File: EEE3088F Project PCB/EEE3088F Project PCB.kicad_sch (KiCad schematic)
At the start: 78 parts, among them IC1 74LVC1G04SE-7, J1 JST PH 2.00mm connector, J3 TYPE-C-31-M-12, SW1 SS12D07VG5 087, U1 DRV8833PWR, U10 LM7805L-TF3-T, U11 TC4056A., U2 DRV8833PWPR, U3 INA219AxD, U4 CH224K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

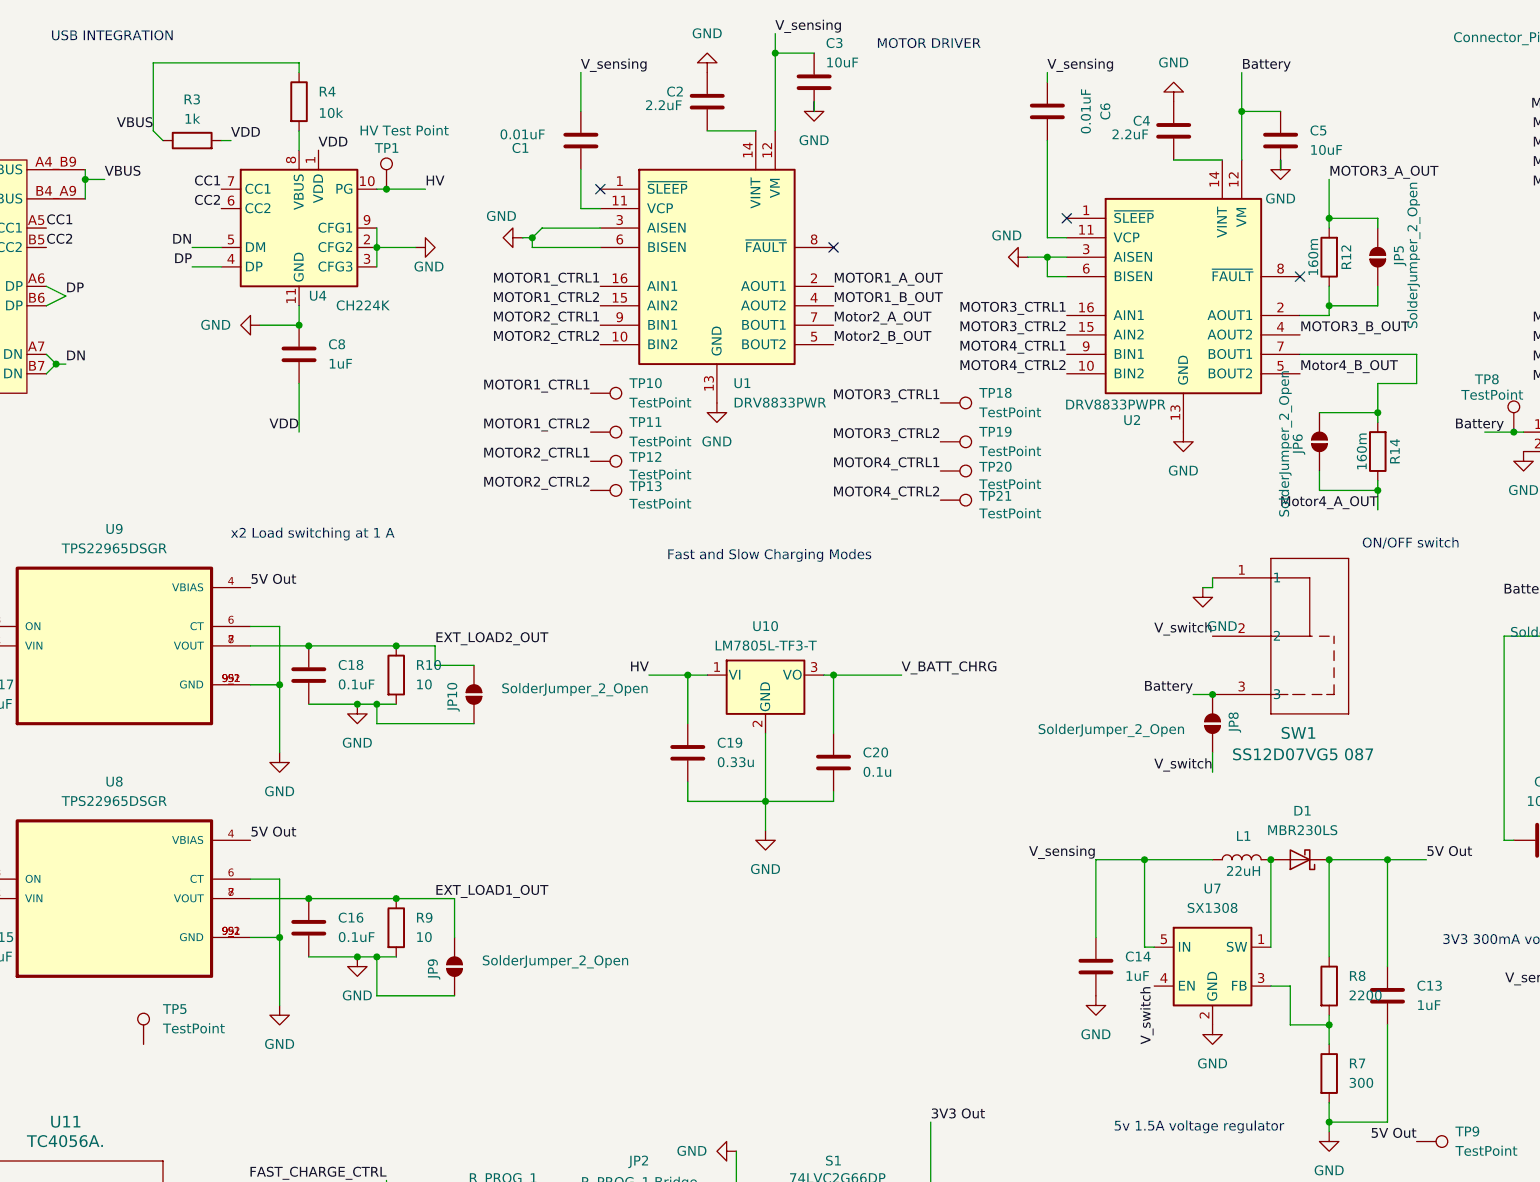
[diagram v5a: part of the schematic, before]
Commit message: Adjusted arrangments on board, and assigned all JLCP part numbers
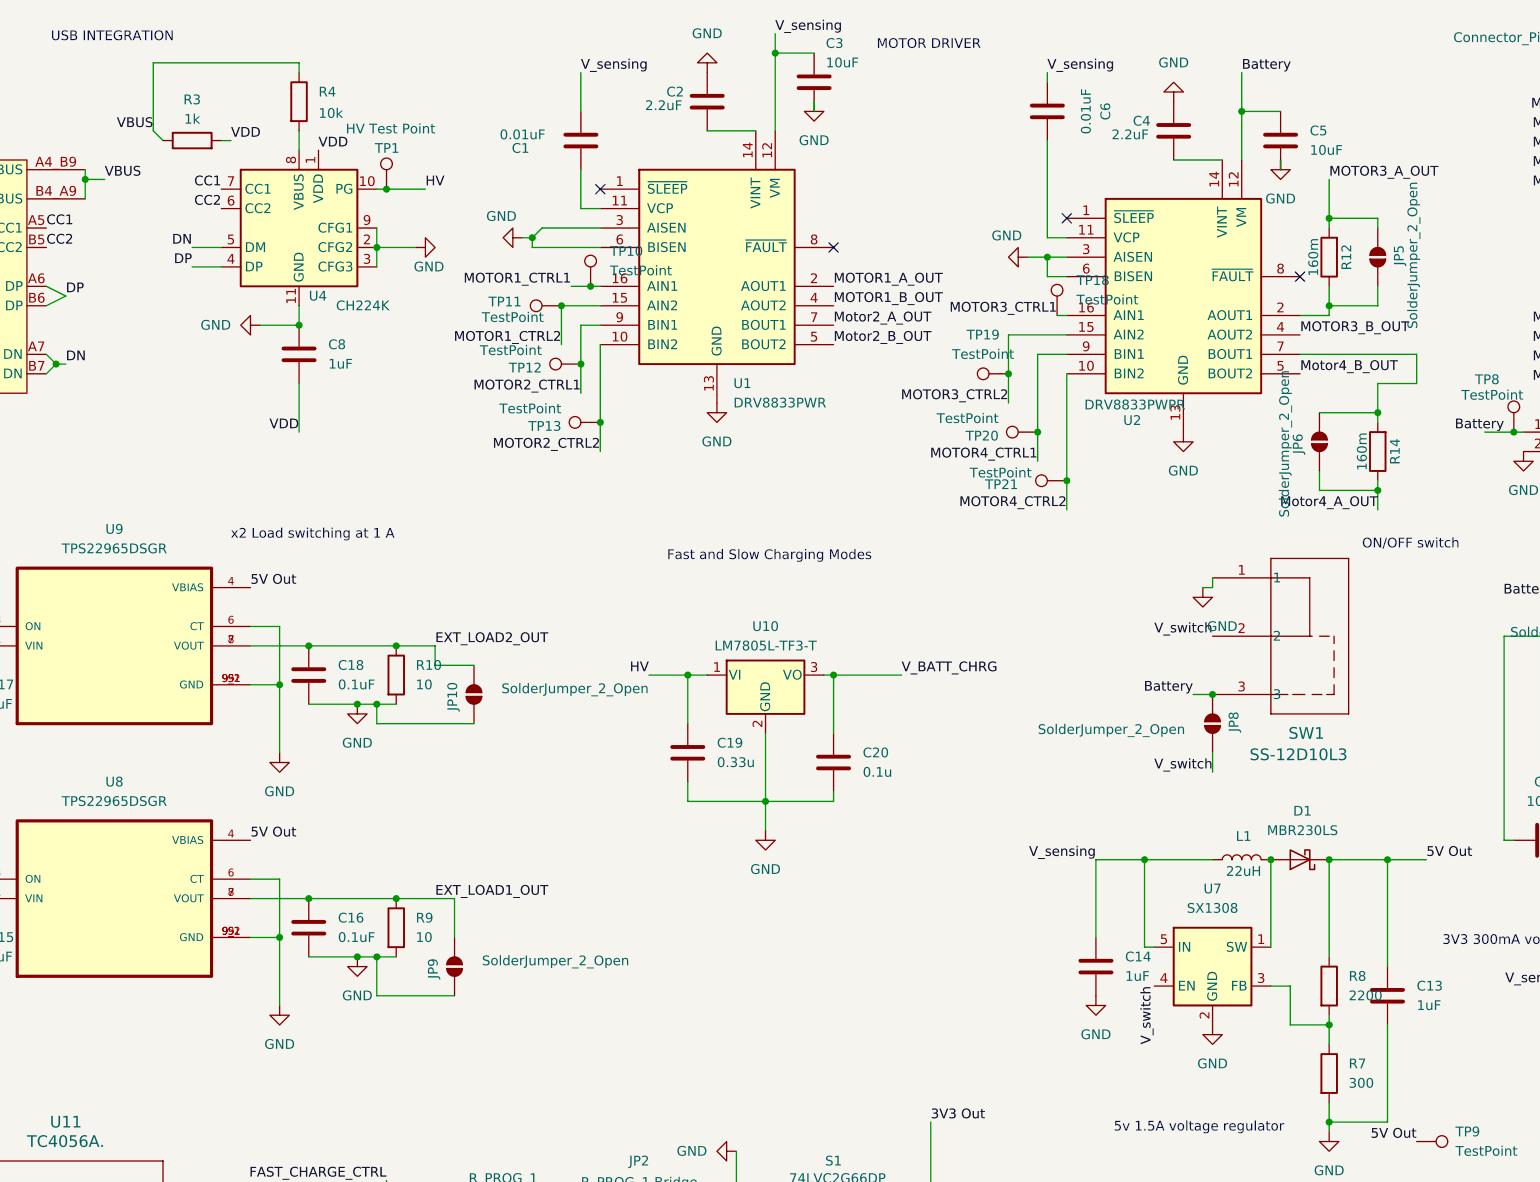
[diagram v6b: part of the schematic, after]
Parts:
- removed TP5: TestPoint, symbol Connector:TestPoint
- SW1: value SS12D07VG5 087 -> SS-12D10L3
- TP10, TP11, TP12, TP13, TP18, TP19, TP20, TP21, TP8: footprint (none) -> TestPoint:TestPoint_Pad_1.0x1.0mm
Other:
- moved on the sheet: TP10, TP11, TP12, TP13, TP18, TP19, TP20, TP21

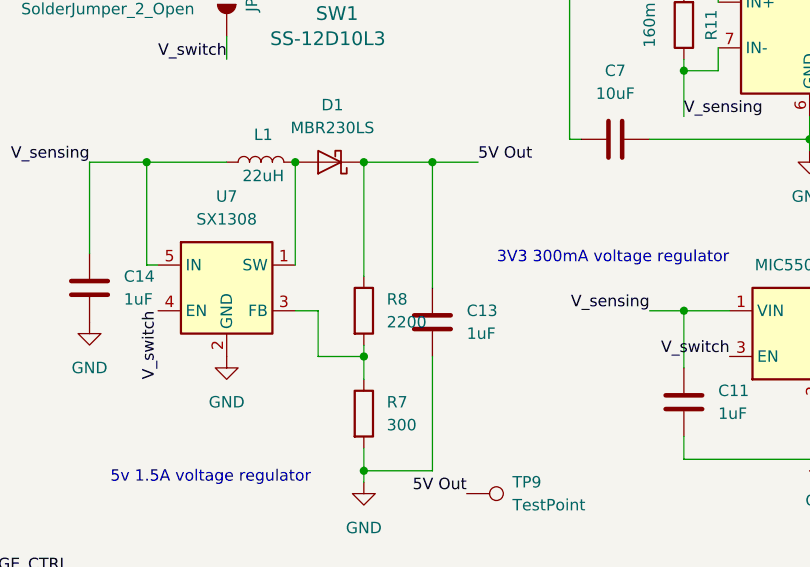
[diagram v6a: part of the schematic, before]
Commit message: adjusted position of 2*16 connector
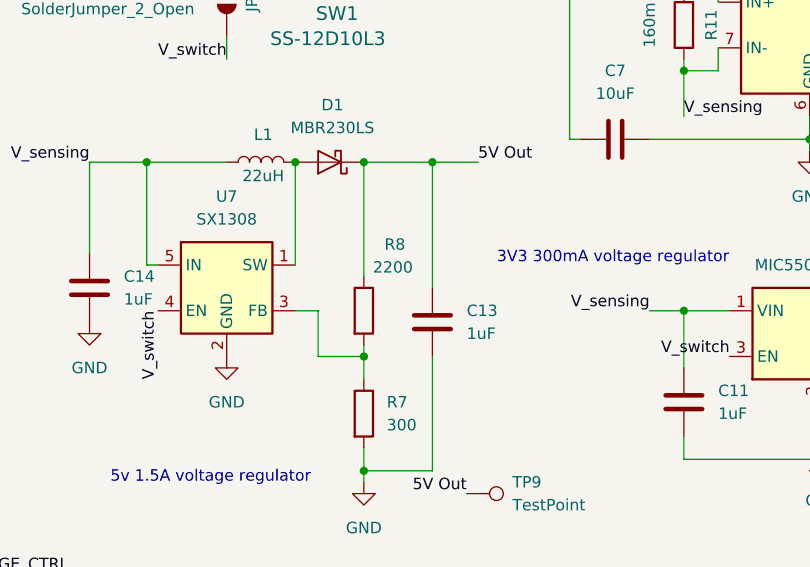
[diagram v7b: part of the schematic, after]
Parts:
- C11, C12, C13, C14, C15, C17: footprint Capacitor_SMD:C_0805_2012Metric_Pad1.18x1.45mm_HandSolder -> exported_footprints:CAPC3216X180N
- C7: footprint Capacitor_SMD:C_0805_2012Metric_Pad1.18x1.45mm_HandSolder -> Capacitor_SMD:C_0402_1005Metric_Pad0.74x0.62mm_HandSolder
- R7: footprint Resistor_SMD:R_0402_1005Metric_Pad0.72x0.64mm_HandSolder -> Resistor_SMD:R_0805_2012Metric_Pad1.20x1.40mm_HandSolder
- R8: footprint Resistor_SMD:R_0402_1005Metric_Pad0.72x0.64mm_HandSolder -> Resistor_SMD:R_0603_1608Metric_Pad0.98x0.95mm_HandSolder
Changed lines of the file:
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@@
 		(polyline
 			(pts
-				(xy 228.6 114.3) (xy 167.64 114.3) (xy 167.64 165.735) (xy 285.75 165.1) (xy 285.75 129.54) (xy 228.6 129.54)
+				(xy 222.25 12.7) (xy 222.25 78.74) (xy 284.48 78.74) (xy 284.48 12.7)
 			)
 			(stroke
@@
 		(polyline
 			(pts
-				(xy 222.25 12.7) (xy 222.25 78.74) (xy 284.48 78.74) (xy 284.48 12.7)
+				(xy 12.7 78.74) (xy 11.43 153.67) (xy 106.68 152.7175) (xy 106.68 78.4225)
 			)
 			(stroke
@@
 		(polyline
 			(pts
-				(xy 167.64 78.74) (xy 167.64 114.3) (xy 228.6 114.3) (xy 228.6 78.74)
+				(xy 93.98 12.7) (xy 93.98 78.74) (xy 222.25 78.74) (xy 222.25 12.7)
 			)
 			(stroke
@@
 		(polyline
 			(pts
-				(xy 93.98 12.7) (xy 93.98 78.74) (xy 222.25 78.74) (xy 222.25 12.7)
+				(xy 167.64 78.74) (xy 167.64 114.3) (xy 228.6 114.3) (xy 228.6 78.74)
 			)
 			(stroke
@@
 		(polyline
 			(pts
-				(xy 12.7 78.74) (xy 11.43 153.67) (xy 106.68 152.7175) (xy 106.68 78.4225)
+				(xy 228.6 114.3) (xy 167.64 114.3) (xy 167.64 165.735) (xy 285.75 165.1) (xy 285.75 129.54) (xy 228.6 129.54)
 			)
 			(stroke
@@
 			)
 		)
-		(property "Footprint" "Capacitor_SMD:C_0805_2012Metric_Pad1.18x1.45mm_HandSolder"
+		(property "Footprint" "exported_footprints:CAPC3216X180N"
 			(at 178.7652 140.97 0)
 			(effects
@@
 			)
 		)
-		(property "Footprint" "Capacitor_SMD:C_0805_2012Metric_Pad1.18x1.45mm_HandSolder"
+		(property "Footprint" "exported_footprints:CAPC3216X180N"
 			(at 28.2448 130.81 0)
 			(effects
@@
 			)
 		)
-		(property "Footprint" "Capacitor_SMD:C_0805_2012Metric_Pad1.18x1.45mm_HandSolder"
+		(property "Footprint" "exported_footprints:CAPC3216X180N"
 			(at 216.8652 144.78 0)
 			(effects
@@
 			)
 		)
-		(property "Footprint" "Capacitor_SMD:C_0805_2012Metric_Pad1.18x1.45mm_HandSolder"
+		(property "Footprint" "exported_footprints:CAPC3216X180N"
 			(at 28.2448 97.79 0)
 			(effects
@@
 			)
 		)
-		(property "Footprint" "Resistor_SMD:R_0402_1005Metric_Pad0.72x0.64mm_HandSolder"
+		(property "Footprint" "Resistor_SMD:R_0805_2012Metric_Pad1.20x1.40mm_HandSolder"
 			(at 206.502 151.13 90)
 			(effects
@@
 			)
 		)
-		(property "Footprint" "Capacitor_SMD:C_0805_2012Metric_Pad1.18x1.45mm_HandSolder"
+		(property "Footprint" "exported_footprints:CAPC3216X180N"
 			(at 272.7452 151.13 0)
 			(effects
@@
 		(on_board yes)
 		(dnp no)
-		(fields_autoplaced yes)
 		(property "Reference" "R8"
-			(at 210.82 138.4299 0)
+			(at 210.566 132.334 0)
 			(effects
 				(font
@@
 		)
 		(property "Value" "2200"
-			(at 210.82 140.9699 0)
+			(at 209.296 134.874 0)
 			(effects
 				(font
@@
 			)
 		)
-		(property "Footprint" "Resistor_SMD:R_0402_1005Metric_Pad0.72x0.64mm_HandSolder"
+		(property "Footprint" "Resistor_SMD:R_0603_1608Metric_Pad0.98x0.95mm_HandSolder"
 			(at 206.502 139.7 90)
 			(effects
@@
 			)
 		)
-		(property "Footprint" "Capacitor_SMD:C_0805_2012Metric_Pad1.18x1.45mm_HandSolder"
+		(property "Footprint" "Capacitor_SMD:C_0402_1005Metric_Pad0.74x0.62mm_HandSolder"
 			(at 240.03 119.6848 0)
 			(effects
@@
 			)
 		)
-		(property "Footprint" "Capacitor_SMD:C_0805_2012Metric_Pad1.18x1.45mm_HandSolder"
+		(property "Footprint" "exported_footprints:CAPC3216X180N"
 			(at 244.8052 153.67 0)
 			(effects
